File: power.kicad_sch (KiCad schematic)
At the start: 1 part, among them U1 CM5104032

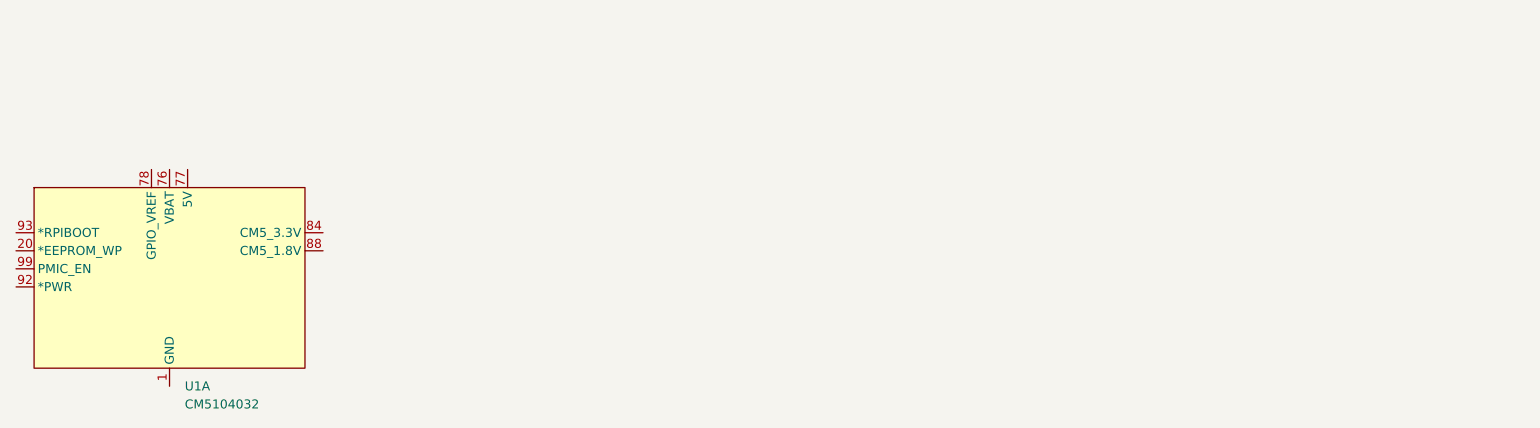
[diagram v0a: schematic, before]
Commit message: added git ignore
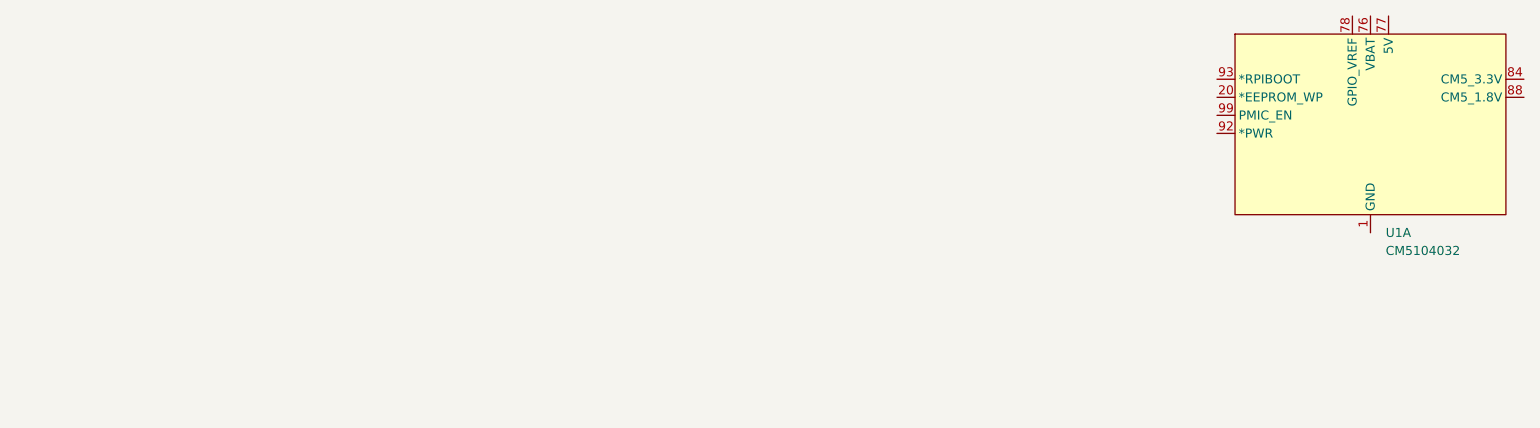
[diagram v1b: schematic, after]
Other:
- moved on the sheet: U1A
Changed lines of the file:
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@@
 	(symbol
 		(lib_id "DIY Pi Smartphone Library:CM5104032")
-		(at 85.09 58.42 0)
+		(at 254 36.83 0)
 		(unit 1)
 		(exclude_from_sim no)
@@
 		(fields_autoplaced yes)
 		(property "Reference" "U1"
-			(at 87.2333 73.66 0)
+			(at 256.1433 52.07 0)
 			(effects
 				(font
@@
 		)
 		(property "Value" "CM5104032"
-			(at 87.2333 76.2 0)
+			(at 256.1433 54.61 0)
 			(effects
 				(font
@@
 		)
 		(property "Footprint" ""
-			(at 85.09 58.42 0)
+			(at 254 36.83 0)
 			(effects
 				(font
@@
 		)
 		(property "Datasheet" ""
-			(at 85.09 58.42 0)
+			(at 254 36.83 0)
 			(effects
 				(font
@@
 		)
 		(property "Description" ""
-			(at 85.09 58.42 0)
+			(at 254 36.83 0)
 			(effects
 				(font

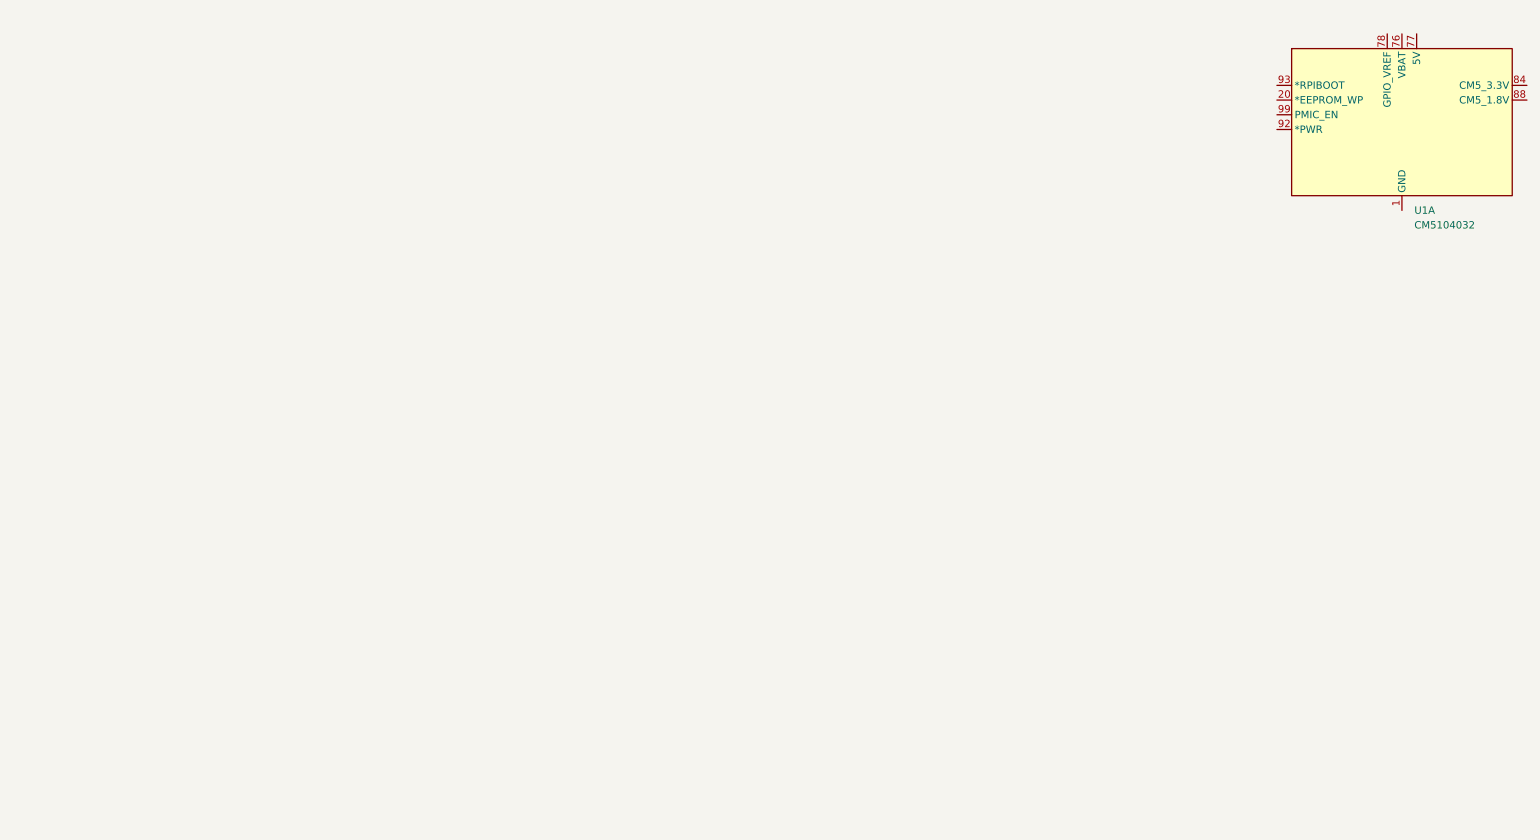
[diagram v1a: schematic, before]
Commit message: added PD TPS65987D and CHG BQ25895
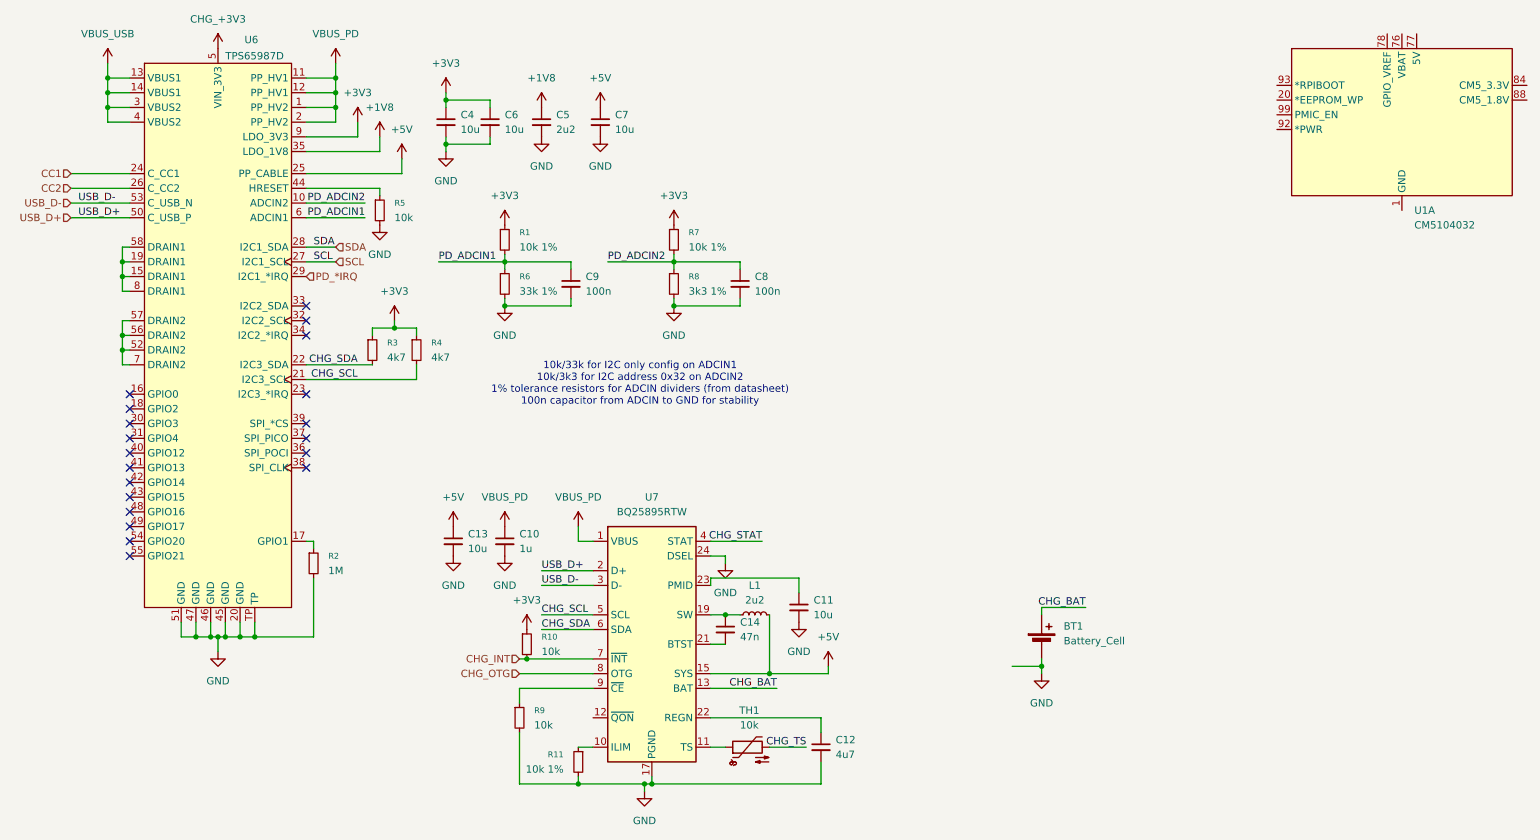
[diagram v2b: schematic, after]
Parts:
- added BT1: Battery_Cell, symbol Device:Battery_Cell
- added C10: 1u, symbol Device:C_Small
- added C11, C13, C4, C6, C7: 10u, symbol Device:C_Small
- added C12: 4u7, symbol Device:C_Small
- added C14: 47n, symbol Device:C_Small
- added C5: 2u2, symbol Device:C_Small
- added C8, C9: 100n, symbol Device:C_Small
- added L1: 2u2, symbol Device:L_Small
- added R1, R11, R7: 10k 1%, symbol Device:R_Small
- added R10, R5, R9: 10k, symbol Device:R_Small
- added R2: 1M, symbol Device:R_Small
- added R3, R4: 4k7, symbol Device:R_Small
- added R6: 33k 1%, symbol Device:R_Small
- added R8: 3k3 1%, symbol Device:R_Small
- added TH1: 10k, symbol Device:Thermistor_NTC
- added U6: TPS65987D, symbol DIY Pi Smartphone Library:TPS65987D
- added U7: BQ25895RTW, Package_DFN_QFN:Texas_RTW_WQFN-24-1EP_4x4mm_P0.5mm_EP2.7x2.7mm_ThermalVias, symbol Battery_Management:BQ25895RTW
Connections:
- net GND: now also BT1.2 (-), C10.2, C11.2, C12.2, C13.2, C4.2, C5.2, C6.2, C7.2, C8.2, C9.2, R11.2, R2.2, R5.2, R6.2, R8.2, R9.2, U6.20 (GND), U6.45 (GND), U6.46 (GND), U6.47 (GND), U6.51 (GND), U6.TP, U7.17 (PGND), U7.18 (PGND), U7.24 (DSEL), U7.25 (PGND)
- new net: R11.1, U7.10 (ILIM)
- new net: TH1.1, U7.11 (TS)
- new net: C14.1, L1.1, U7.19 (SW), U7.20 (SW)
- new net: C14.2, U7.21 (BTST)
- new net: C12.1, U7.22 (REGN)
- new net: C11.1, U7.23 (PMID)
- new net: R9.1, U7.9 (~{CE})
- new net: R5.1, U6.44 (HRESET)
- new net: R2.1, U6.17 (GPIO1)
- new net: U6.15 (DRAIN1), U6.19 (DRAIN1), U6.58 (DRAIN1), U6.8 (DRAIN1)
- new net: U6.52 (DRAIN2), U6.56 (DRAIN2), U6.57 (DRAIN2), U6.7 (DRAIN2)
- new net +1V8: C5.1, U6.35 (LDO_1V8)
- new net +3V3: C4.1, C6.1, R1.1, R10.1, R3.1, R4.1, R7.1, U6.9 (LDO_3V3)
- new net +5V: C13.1, C7.1, L1.2, U6.25 (PP_CABLE), U7.15 (SYS), U7.16 (SYS)
- new net CC1: U6.24 (C_CC1)
- new net CC2: U6.26 (C_CC2)
- new net CHG_+3V3: U6.5 (VIN_3V3)
- new net CHG_BAT: BT1.1 (+), U7.13 (BAT), U7.14 (BAT)
- new net CHG_INT: R10.2, U7.7 (~{INT})
- new net CHG_OTG: U7.8 (OTG)
- new net CHG_SCL: R4.2, U6.21 (I2C3_SCL), U7.5 (SCL)
- new net CHG_SDA: R3.2, U6.22 (I2C3_SDA), U7.6 (SDA)
- new net CHG_STAT: U7.4 (STAT)
- new net CHG_TS: TH1.2
- new net PD_*IRQ: U6.29 (I2C1_*IRQ)
- new net PD_ADCIN1: C9.1, R1.2, R6.1, U6.6 (ADCIN1)
- new net PD_ADCIN2: C8.1, R7.2, R8.1, U6.10 (ADCIN2)
- new net SCL: U6.27 (I2C1_SCL)
- new net SDA: U6.28 (I2C1_SDA)
- new net USB_D+: U6.50 (C_USB_P), U7.2 (D+)
- new net USB_D-: U6.53 (C_USB_N), U7.3 (D-)
- new net VBUS_PD: C10.1, U6.1 (PP_HV2), U6.11 (PP_HV1), U6.12 (PP_HV1), U6.2 (PP_HV2), U7.1 (VBUS)
- new net VBUS_USB: U6.13 (VBUS1), U6.14 (VBUS1), U6.3 (VBUS2), U6.4 (VBUS2)
- no-connect marks 0 -> 20
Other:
- note added: "10k/33k for I2C only config on ADCIN1 10k/3k3 for I2C address 0x32 on ADCIN2 1% tolerance resistors for ADCIN dividers (from datasheet) 100n capacitor from ADCIN to GND for stability"

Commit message: added MAX177330 CHG
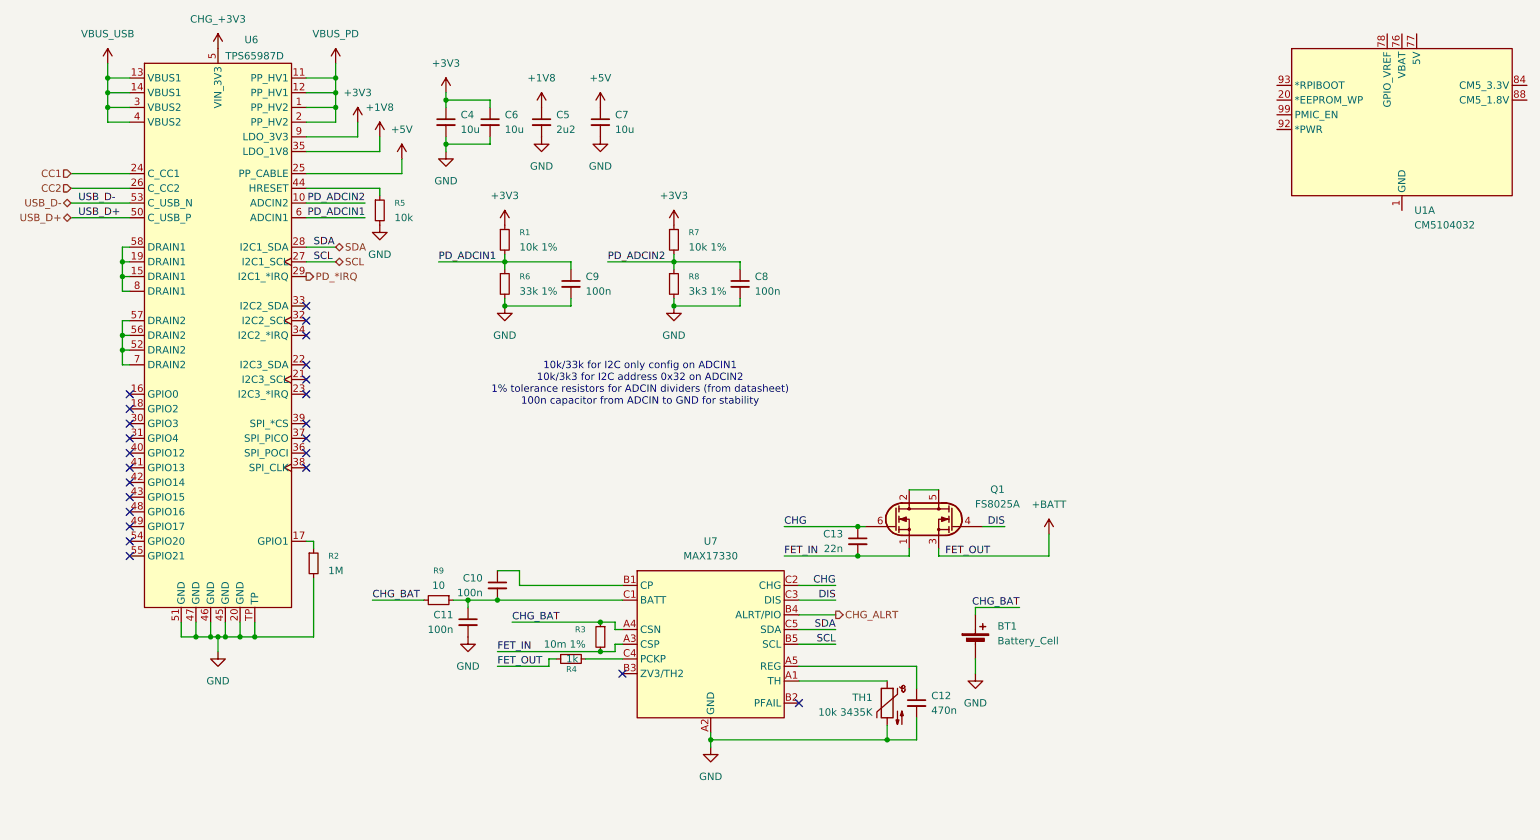
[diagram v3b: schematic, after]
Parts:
- removed C14: 47n, symbol Device:C_Small
- removed L1: 2u2, symbol Device:L_Small
- removed R10: 10k, symbol Device:R_Small
- removed R11: 10k 1%, symbol Device:R_Small
- removed U7: BQ25895RTW, Package_DFN_QFN:Texas_RTW_WQFN-24-1EP_4x4mm_P0.5mm_EP2.7x2.7mm_ThermalVias, symbol Battery_Management:BQ25895RTW
- added Q1: FS8025A, symbol PCM_Transistor_MOSFET_AKL:Q_NMOS-E_DUAL_Generic_S1DS2G2DG1
- added U7: MAX17330, symbol DIY Pi Smartphone Library:MAX17330
- C10: value 1u -> 100n
- C11: value 10u -> 100n
- C12: value 4u7 -> 470n
- C13: value 10u -> 22n
- R3: value 4k7 -> 10m 1%
- R4: value 4k7 -> 1k
- R9: value 10k -> 10
- TH1: value 10k -> 10k 3435K
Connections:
- net CHG_TS is gone; now on net GND: TH1.2
- net +3V3: no longer R3.1, R4.1
- net +5V: no longer C13.1
- net CHG_BAT: now also R3.1, R9.2, U7.A4 (CSN)
- net GND: now also U7.A2 (GND); no longer C10.2, C13.2, R9.2
- net SCL: now also U7.B5 (SCL)
- net SDA: now also U7.C5 (SDA)
- net VBUS_PD: no longer C10.1
- net at TH1.1: now also U7.A1 (TH)
- net at C12.1: now also U7.A5 (REG)
- net at C11.1: now also C10.2, R9.1, U7.C1 (BATT)
- net CHG_SCL: no longer names the net of R4.2
- net CHG_SCL: now also U7.C4 (PCKP); no longer U6.21 (I2C3_SCL)
- net CHG_SDA: no longer names the net of U6.22 (I2C3_SDA)
- net CHG_SDA: no longer R3.2
- new net: C10.1, U7.B1 (CP)
- new net: Q1.2 (D1), Q1.5 (D2)
- new net +BATT: Q1.3 (S2), R4.1
- new net CHG: C13.1, Q1.6 (G1), U7.C2 (CHG)
- new net CHG_ALRT: U7.B4 (ALRT/PIO)
- new net DIS: Q1.4 (G2), U7.C3 (DIS)
- new net FET_IN: C13.2, Q1.1 (S1), R3.2, U7.A3 (CSP)
- no-connect marks 20 -> 24
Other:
- moved on the sheet: BT1
